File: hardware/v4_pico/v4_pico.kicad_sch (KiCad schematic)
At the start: 103 parts, among them J1 joystick, J10 ON/OFF, J11 MIDI IN bk: 5 R: 4, J2 LED strip, J3 SSD1306 SPI, J4 MIDI OUT Y:M5 - R:M4, J5 Batt, J6 Neck - Y:O BK:B R:3.3, J7 01x03, J8 MXP5010, J9 Thumb, Q1 2N7000, SW1 SW_DIP_x01, U1 74HC165, U2 74HC165, U3 74HC165, U4 Pico, U5 FJ08K, U6 6N138, U7 MCP3002

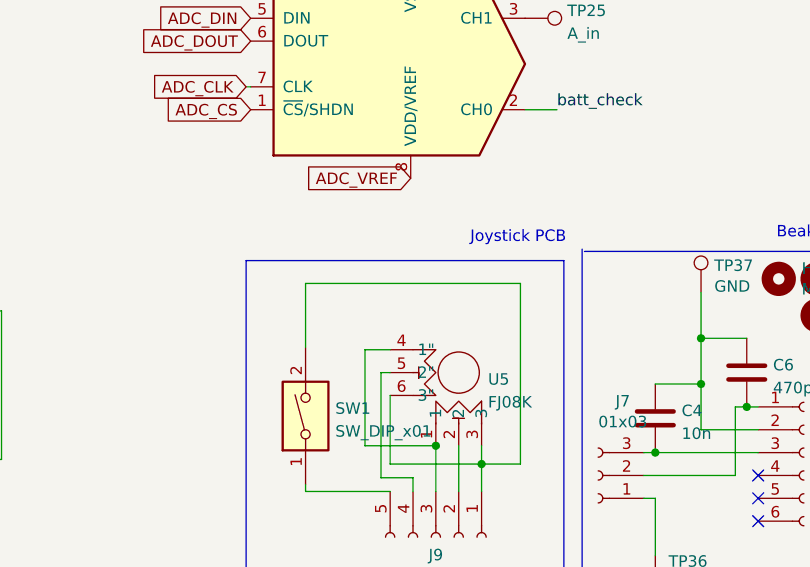
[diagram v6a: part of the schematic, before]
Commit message: Check on courtyarb, placing
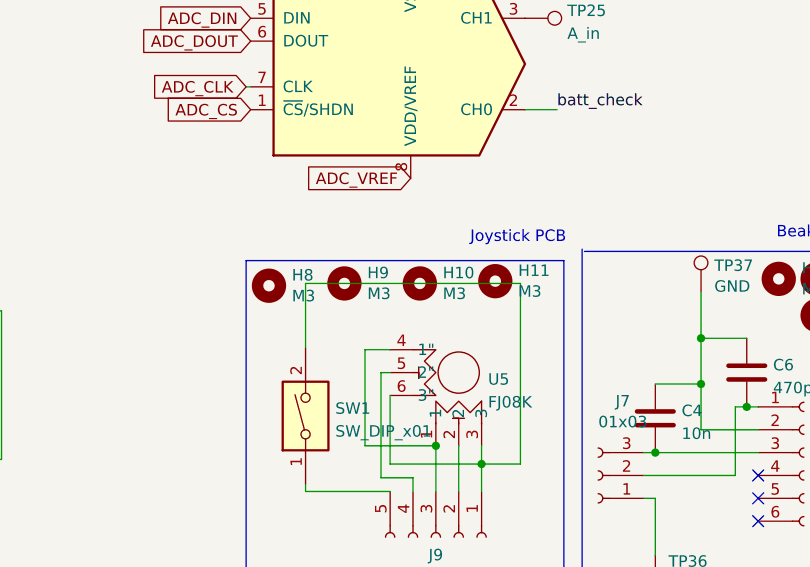
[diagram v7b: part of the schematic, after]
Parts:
- added H10, H11, H8, H9: M3, MountingHole:MountingHole_3.2mm_M3_ISO14580, symbol Mechanical:MountingHole
- H3, H4, H5, H6, H7: footprint MountingHole:MountingHole_3.2mm_M3 -> MountingHole:MountingHole_3.2mm_M3_ISO14580
- J9: footprint Connector_JST:JST_PH_B5B-PH-K_1x05_P2.00mm_Vertical -> Connector_JST:JST_PH_S5B-PH-K_1x05_P2.00mm_Horizontal
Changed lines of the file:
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@@
       (effects (font (size 1.27 1.27)) (justify left))
     )
-    (property "Footprint" "MountingHole:MountingHole_3.2mm_M3" (id 2) (at 171.45 186.944 0)
+    (property "Footprint" "MountingHole:MountingHole_3.2mm_M3_ISO14580" (id 2) (at 171.45 186.944 0)
       (effects (font (size 1.27 1.27)) hide)
     )
@@
       (effects (font (size 1.27 1.27)) (justify left))
     )
-    (property "Footprint" "MountingHole:MountingHole_3.2mm_M3" (id 2) (at 171.45 194.564 0)
+    (property "Footprint" "MountingHole:MountingHole_3.2mm_M3_ISO14580" (id 2) (at 171.45 194.564 0)
       (effects (font (size 1.27 1.27)) hide)
     )
@@
       (effects (font (size 1.27 1.27)) (justify left))
     )
-    (property "Footprint" "MountingHole:MountingHole_3.2mm_M3" (id 2) (at 273.812 124.714 0)
+    (property "Footprint" "MountingHole:MountingHole_3.2mm_M3_ISO14580" (id 2) (at 273.812 124.714 0)
       (effects (font (size 1.27 1.27)) hide)
     )
@@
     (pin "1")
   )
+  (symbol (lib_id "Mechanical:MountingHole") (at 225.552 125.222 0) (unit 1)
+    (in_bom yes) (on_board yes)
+    (property "Reference" "H9" (id 0) (at 228.092 124.0536 0)
+      (effects (font (size 1.27 1.27)) (justify left))
+    )
+    (property "Value" "M3" (id 1) (at 228.092 126.365 0)
+      (effects (font (size 1.27 1.27)) (justify left))
+    )
+    (property "Footprint" "MountingHole:MountingHole_3.2mm_M3_ISO14580" (id 2) (at 225.552 125.222 0)
+      (effects (font (size 1.27 1.27)) hide)
+    )
+    (property "Datasheet" "~" (id 3) (at 225.552 125.222 0)
+      (effects (font (size 1.27 1.27)) hide)
+    )
+  )
   (symbol (lib_id "Device:C") (at 270.256 135.128 0) (unit 1)
     (in_bom yes) (on_board yes) (fields_autoplaced)
@@
       (effects (font (size 1.27 1.27)) (justify left))
     )
-    (property "Footprint" "MountingHole:MountingHole_3.2mm_M3" (id 2) (at 163.068 187.198 0)
+    (property "Footprint" "MountingHole:MountingHole_3.2mm_M3_ISO14580" (id 2) (at 163.068 187.198 0)
       (effects (font (size 1.27 1.27)) hide)
     )
@@
     (pin "7")
     (pin "8")
+  )
+  (symbol (lib_id "Mechanical:MountingHole") (at 233.934 125.222 0) (unit 1)
+    (in_bom yes) (on_board yes)
+    (property "Reference" "H10" (id 0) (at 236.474 124.0536 0)
+      (effects (font (size 1.27 1.27)) (justify left))
+    )
+    (property "Value" "M3" (id 1) (at 236.474 126.365 0)
+      (effects (font (size 1.27 1.27)) (justify left))
+    )
+    (property "Footprint" "MountingHole:MountingHole_3.2mm_M3_ISO14580" (id 2) (at 233.934 125.222 0)
+      (effects (font (size 1.27 1.27)) hide)
+    )
+    (property "Datasheet" "~" (id 3) (at 233.934 125.222 0)
+      (effects (font (size 1.27 1.27)) hide)
+    )
   )
   (symbol (lib_id "power:+3.3V") (at 174.498 77.724 180) (unit 1)
@@
       (effects (font (size 1.27 1.27)) (justify left))
     )
-    (property "Footprint" "MountingHole:MountingHole_3.2mm_M3" (id 2) (at 163.068 194.818 0)
+    (property "Footprint" "MountingHole:MountingHole_3.2mm_M3_ISO14580" (id 2) (at 163.068 194.818 0)
       (effects (font (size 1.27 1.27)) hide)
     )
@@
     (property "Reference" "J9" (id 0) (at 235.712 155.3956 90))
     (property "Value" "Thumb" (id 1) (at 235.712 157.9325 90))
-    (property "Footprint" "Connector_JST:JST_PH_B5B-PH-K_1x05_P2.00mm_Vertical" (id 2) (at 235.712 153.416 0)
+    (property "Footprint" "Connector_JST:JST_PH_S5B-PH-K_1x05_P2.00mm_Horizontal" (id 2) (at 235.712 153.416 0)
       (effects (font (size 1.27 1.27)) hide)
     )
@@
     (pin "3")
   )
+  (symbol (lib_id "Mechanical:MountingHole") (at 217.17 125.476 0) (unit 1)
+    (in_bom yes) (on_board yes)
+    (property "Reference" "H8" (id 0) (at 219.71 124.3076 0)
+      (effects (font (size 1.27 1.27)) (justify left))
+    )
+    (property "Value" "M3" (id 1) (at 219.71 126.619 0)
+      (effects (font (size 1.27 1.27)) (justify left))
+    )
+    (property "Footprint" "MountingHole:MountingHole_3.2mm_M3_ISO14580" (id 2) (at 217.17 125.476 0)
+      (effects (font (size 1.27 1.27)) hide)
+    )
+    (property "Datasheet" "~" (id 3) (at 217.17 125.476 0)
+      (effects (font (size 1.27 1.27)) hide)
+    )
+  )
   (symbol (lib_id "power:PWR_FLAG") (at 269.24 37.592 0) (unit 1)
     (in_bom yes) (on_board yes) (fields_autoplaced)
@@
     )
     (pin "1")
+  )
+  (symbol (lib_id "Mechanical:MountingHole") (at 242.316 124.968 0) (unit 1)
+    (in_bom yes) (on_board yes)
+    (property "Reference" "H11" (id 0) (at 244.856 123.7996 0)
+      (effects (font (size 1.27 1.27)) (justify left))
+    )
+    (property "Value" "M3" (id 1) (at 244.856 126.111 0)
+      (effects (font (size 1.27 1.27)) (justify left))
+    )
+    (property "Footprint" "MountingHole:MountingHole_3.2mm_M3_ISO14580" (id 2) (at 242.316 124.968 0)
+      (effects (font (size 1.27 1.27)) hide)
+    )
+    (property "Datasheet" "~" (id 3) (at 242.316 124.968 0)
+      (effects (font (size 1.27 1.27)) hide)
+    )
   )
   (symbol (lib_id "power:GND") (at 43.18 66.04 0) (unit 1)
@@
     )
     (path "/00000000-0000-0000-0000-000061ca8909"
-      (reference "H3") (unit 1) (value "M3") (footprint "MountingHole:MountingHole_3.2mm_M3")
+      (reference "H3") (unit 1) (value "M3") (footprint "MountingHole:MountingHole_3.2mm_M3_ISO14580")
     )
     (path "/00000000-0000-0000-0000-000061ca990c"
-      (reference "H4") (unit 1) (value "M3") (footprint "MountingHole:MountingHole_3.2mm_M3")
+      (reference "H4") (unit 1) (value "M3") (footprint "MountingHole:MountingHole_3.2mm_M3_ISO14580")
     )
     (path "/00000000-0000-0000-0000-000061cc6588"
-      (reference "H5") (unit 1) (value "M3") (footprint "MountingHole:MountingHole_3.2mm_M3")
+      (reference "H5") (unit 1) (value "M3") (footprint "MountingHole:MountingHole_3.2mm_M3_ISO14580")
     )
     (path "/2d002a73-5516-4c7c-a5de-f495a513c854"
-      (reference "H6") (unit 1) (value "M3") (footprint "MountingHole:MountingHole_3.2mm_M3")
+      (reference "H6") (unit 1) (value "M3") (footprint "MountingHole:MountingHole_3.2mm_M3_ISO14580")
     )
     (path "/c3c77499-0c99-48fd-98c8-a98114e8d5ad"
-      (reference "H7") (unit 1) (value "M3") (footprint "MountingHole:MountingHole_3.2mm_M3")
+      (reference "H7") (unit 1) (value "M3") (footprint "MountingHole:MountingHole_3.2mm_M3_ISO14580")
+    )
+    (path "/de70908c-6b19-4a63-8809-f2cda5024014"
+      (reference "H8") (unit 1) (value "M3") (footprint "MountingHole:MountingHole_3.2mm_M3_ISO14580")
+    )
+    (path "/038b6cb6-26ff-442c-af99-baf8324b6379"
+      (reference "H9") (unit 1) (value "M3") (footprint "MountingHole:MountingHole_3.2mm_M3_ISO14580")
+    )
+    (path "/3f7b66fe-58aa-4ee1-8afe-8b5a627eb84f"
+      (reference "H10") (unit 1) (value "M3") (footprint "MountingHole:MountingHole_3.2mm_M3_ISO14580")
+    )
+    (path "/f19486a2-0dbc-4306-85cf-ddb670516198"
+      (reference "H11") (unit 1) (value "M3") (footprint "MountingHole:MountingHole_3.2mm_M3_ISO14580")
     )
     (path "/00000000-0000-0000-0000-000061c0fcb8"
@@
     )
     (path "/c8ced3b0-fe5a-44bd-8b6d-d442a8ca2e6b"
-      (reference "J9") (unit 1) (value "Thumb") (footprint "Connector_JST:JST_PH_B5B-PH-K_1x05_P2.00mm_Vertical")
+      (reference "J9") (unit 1) (value "Thumb") (footprint "Connector_JST:JST_PH_S5B-PH-K_1x05_P2.00mm_Horizontal")
     )
     (path "/51855148-c4cd-4659-9355-2a7b71541229"

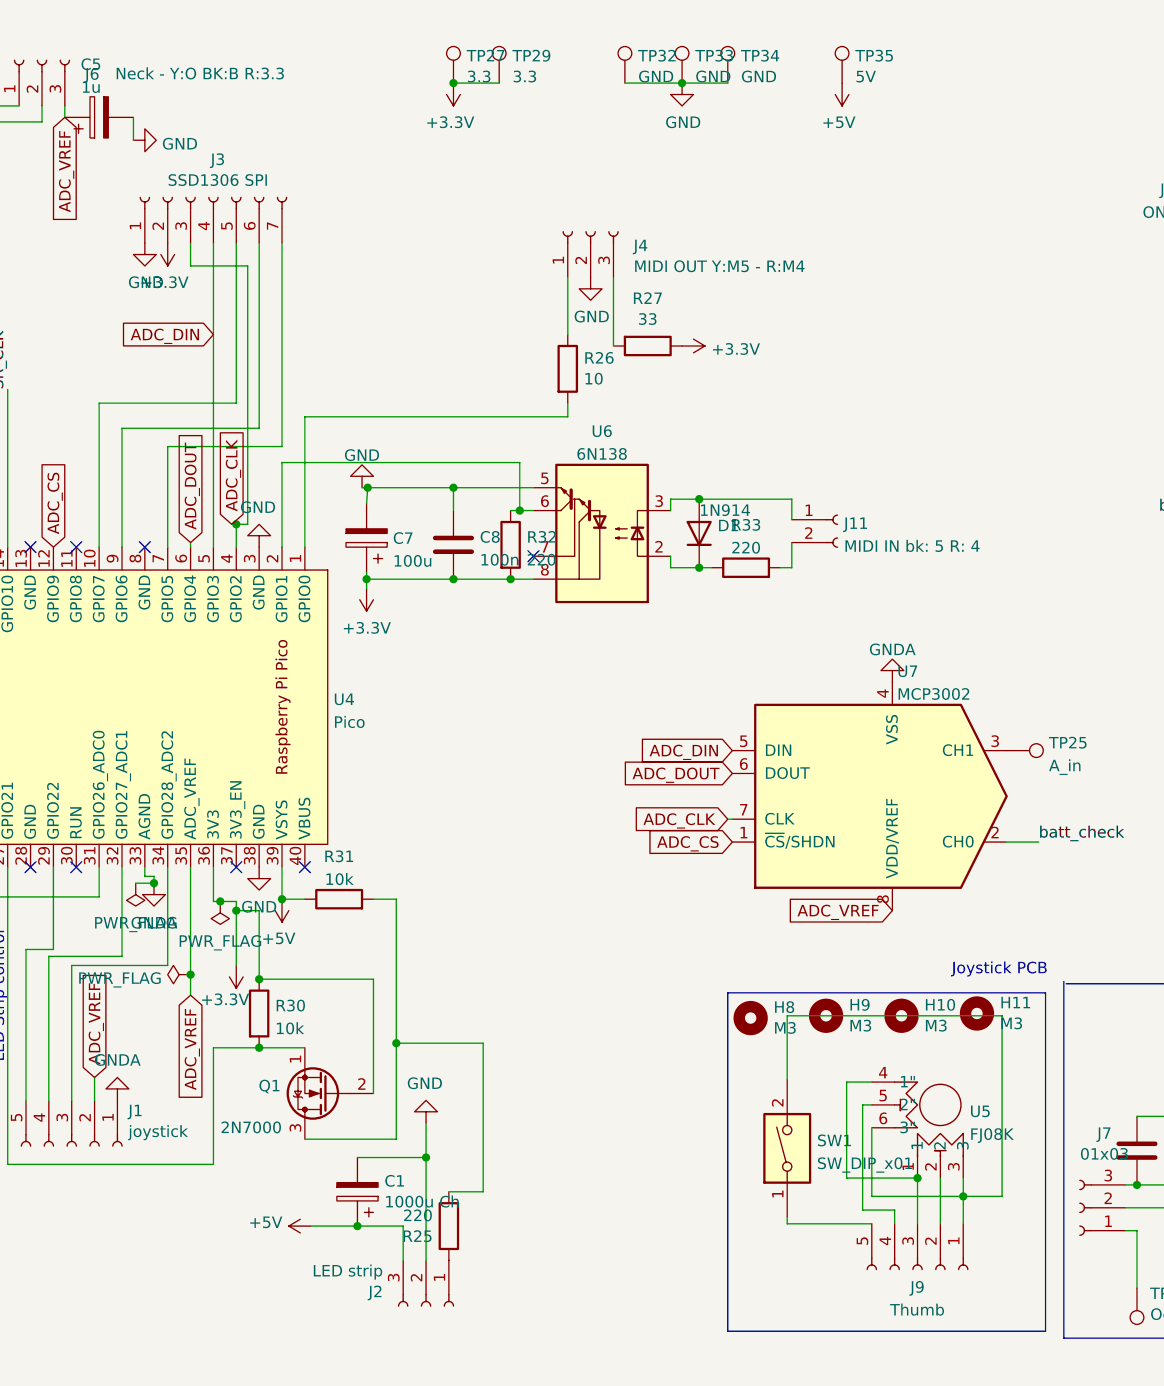
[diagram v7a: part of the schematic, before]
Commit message: PCB cured and routed
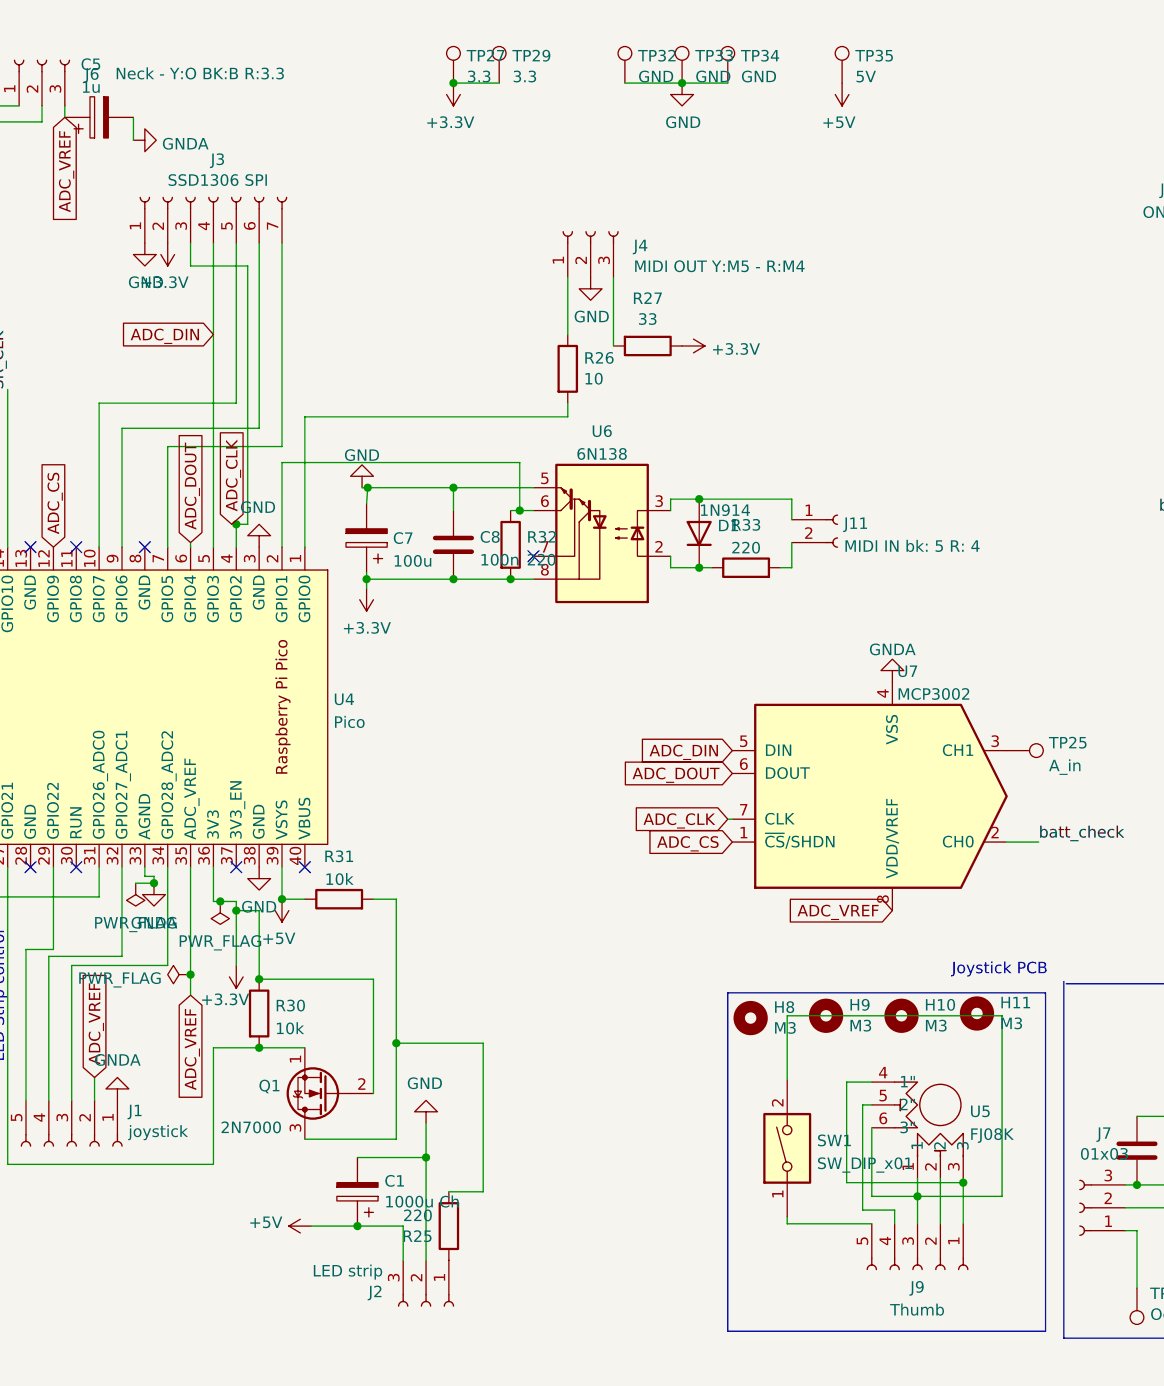
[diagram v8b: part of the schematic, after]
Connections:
- net GND: no longer C5.2
- net GNDA: now also C5.2
- net at SW1.2, U5.6 (3"): now also J9.3 (Pin_3), U5.1; no longer J9.1 (Pin_1), U5.3
- new net: J9.1 (Pin_1), U5.3, U5.4 (1")
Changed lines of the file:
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@@
 (kicad_sch (version 20211123) (generator eeschema)
   (paper "A4")
+  (junction (at 235.712 145.288) (diameter 0) (color 0 0 0 0)
+  )
   (junction (at 48.26 106.68) (diameter 0) (color 0 0 0 0)
   )
@@
   (junction (at 184.15 21.59) (diameter 0) (color 0 0 0 0)
   )
-  (junction (at 235.712 143.256) (diameter 0) (color 0 0 0 0)
-  )
   (junction (at 190.5 76.708) (diameter 0) (color 0 0 0 0)
   )
@@
   (junction (at 67.31 104.14) (diameter 0) (color 0 0 0 0)
   )
+  (junction (at 240.792 143.764) (diameter 0) (color 0 0 0 0)
+  )
   (junction (at 49.53 165.1) (diameter 0) (color 0 0 0 0)
   )
@@
   (junction (at 150.876 110.49) (diameter 0) (color 0 0 0 0)
   )
-  (junction (at 240.792 145.288) (diameter 0) (color 0 0 0 0)
-  )
   (junction (at 209.55 21.59) (diameter 0) (color 0 0 0 0)
   )
@@
     (stroke (width 0) (type default) (color 0 0 0 0))
   )
-  (wire (pts (xy 227.838 143.256) (xy 227.838 132.588))
+  (wire (pts (xy 227.838 143.764) (xy 227.838 132.588))
     (stroke (width 0) (type default) (color 0 0 0 0))
   )
@@
     (stroke (width 0) (type default) (color 0 0 0 0))
   )
-  (wire (pts (xy 240.792 145.288) (xy 240.792 143.256))
-    (stroke (width 0) (type default) (color 0 0 0 0))
-  )
   (wire (pts (xy 67.31 15.24) (xy 67.31 33.02))
     (stroke (width 0) (type default) (color 0 0 0 0))
@@
     (stroke (width 0) (type default) (color 0 0 0 0))
   )
+  (wire (pts (xy 240.792 143.764) (xy 240.792 143.256))
+    (stroke (width 0) (type default) (color 0 0 0 0))
+  )
   (wire (pts (xy 174.498 76.708) (xy 174.498 77.724))
     (stroke (width 0) (type default) (color 0 0 0 0))
@@
     (stroke (width 0) (type default) (color 0 0 0 0))
   )
-  (wire (pts (xy 235.712 143.256) (xy 235.712 148.336))
+  (wire (pts (xy 235.712 143.256) (xy 235.712 145.288))
     (stroke (width 0) (type default) (color 0 0 0 0))
   )
@@
     (stroke (width 0) (type default) (color 0 0 0 0))
   )
+  (wire (pts (xy 235.712 145.288) (xy 235.712 148.336))
+    (stroke (width 0) (type default) (color 0 0 0 0))
+  )
   (wire (pts (xy 162.56 39.37) (xy 162.56 59.944))
     (stroke (width 0) (type default) (color 0 0 0 0))
@@
     (stroke (width 0) (type default) (color 0 0 0 0))
   )
+  (wire (pts (xy 240.792 143.764) (xy 240.792 148.336))
+    (stroke (width 0) (type default) (color 0 0 0 0))
+  )
   (wire (pts (xy 72.39 77.47) (xy 102.87 77.47))
     (stroke (width 0) (type default) (color 0 0 0 0))
@@
     (stroke (width 0) (type default) (color 0 0 0 0))
   )
+  (wire (pts (xy 230.632 145.288) (xy 235.712 145.288))
+    (stroke (width 0) (type default) (color 0 0 0 0))
+  )
   (wire (pts (xy 141.732 134.62) (xy 141.732 119.634))
     (stroke (width 0) (type default) (color 0 0 0 0))
@@
     (stroke (width 0) (type default) (color 0 0 0 0))
   )
-  (wire (pts (xy 240.792 145.288) (xy 240.792 148.336))
-    (stroke (width 0) (type default) (color 0 0 0 0))
-  )
   (wire (pts (xy 165.1 39.37) (xy 165.1 61.976))
     (stroke (width 0) (type default) (color 0 0 0 0))
@@
     (stroke (width 0) (type default) (color 0 0 0 0))
   )
-  (wire (pts (xy 245.11 145.288) (xy 240.792 145.288))
-    (stroke (width 0) (type default) (color 0 0 0 0))
-  )
   (wire (pts (xy 19.05 185.42) (xy 72.39 185.42))
     (stroke (width 0) (type default) (color 0 0 0 0))
@@
     (stroke (width 0) (type default) (color 0 0 0 0))
   )
-  (wire (pts (xy 235.712 143.256) (xy 227.838 143.256))
+  (wire (pts (xy 235.712 145.288) (xy 245.11 145.288))
     (stroke (width 0) (type default) (color 0 0 0 0))
   )
@@
     (stroke (width 0) (type default) (color 0 0 0 0))
   )
-  (wire (pts (xy 230.632 145.288) (xy 240.792 145.288))
-    (stroke (width 0) (type default) (color 0 0 0 0))
-  )
   (wire (pts (xy 150.876 109.728) (xy 150.876 110.49))
     (stroke (width 0) (type default) (color 0 0 0 0))
@@
     (stroke (width 0) (type default) (color 0 0 0 0))
   )
+  (wire (pts (xy 227.838 143.764) (xy 240.792 143.764))
+    (stroke (width 0) (type default) (color 0 0 0 0))
+  )
   (wire (pts (xy 64.77 33.02) (xy 67.31 33.02))
     (stroke (width 0) (type default) (color 0 0 0 0))
@@
     (pin "2")
   )
-  (symbol (lib_name "GND_4") (lib_id "power:GND") (at 148.59 27.94 90) (unit 1)
-    (in_bom yes) (on_board yes) (fields_autoplaced)
-    (property "Reference" "#PWR02" (id 0) (at 154.94 27.94 0)
-      (effects (font (size 1.27 1.27)) hide)
-    )
-    (property "Value" "GND" (id 1) (at 151.765 28.3738 90)
-      (effects (font (size 1.27 1.27)) (justify right))
-    )
-    (property "Footprint" "" (id 2) (at 148.59 27.94 0)
-      (effects (font (size 1.27 1.27)) hide)
-    )
-    (property "Datasheet" "" (id 3) (at 148.59 27.94 0)
-      (effects (font (size 1.27 1.27)) hide)
-    )
-    (pin "1")
-  )
   (symbol (lib_id "Device:C") (at 260.096 140.208 0) (unit 1)
     (in_bom yes) (on_board yes) (fields_autoplaced)
@@
     (pin "1")
   )
+  (symbol (lib_id "power:GNDA") (at 148.59 27.94 90) (unit 1)
+    (in_bom yes) (on_board yes) (fields_autoplaced)
+    (property "Reference" "#PWR?" (id 0) (at 154.94 27.94 0)
+      (effects (font (size 1.27 1.27)) hide)
+    )
+    (property "Value" "GNDA" (id 1) (at 151.765 28.3738 90)
+      (effects (font (size 1.27 1.27)) (justify right))
+    )
+    (property "Footprint" "" (id 2) (at 148.59 27.94 0)
+      (effects (font (size 1.27 1.27)) hide)
+    )
+    (property "Datasheet" "" (id 3) (at 148.59 27.94 0)
+      (effects (font (size 1.27 1.27)) hide)
+    )
+    (pin "1")
+  )
   (symbol (lib_id "Mechanical:MountingHole") (at 242.316 124.968 0) (unit 1)
     (in_bom yes) (on_board yes)
@@
       (reference "#PWR01") (unit 1) (value "GNDA") (footprint "")
     )
-    (path "/97bfdb0a-bb4a-45fb-929e-6966632074c2"
-      (reference "#PWR02") (unit 1) (value "GND") (footprint "")
-    )
     (path "/f766c224-94b0-421f-98c8-1d142ec2e101"
       (reference "#PWR03") (unit 1) (value "GNDA") (footprint "")
@@
       (reference "#PWR0129") (unit 1) (value "GND") (footprint "")
     )
+    (path "/e4a37a73-5dce-40fb-a479-052c7cfe6105"
+      (reference "#PWR?") (unit 1) (value "GNDA") (footprint "")
+    )
     (path "/00000000-0000-0000-0000-000061cbc345"
